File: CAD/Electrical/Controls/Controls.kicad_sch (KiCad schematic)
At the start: 31 parts, among them J1 Aileron Servo, J10 Battery and/or BMS, J11 Restart/Boot Button, J12 GPS, J13 Cadence Sensor, J14 Gyroscope, J15 LCD, J16 pitot tube assembly, J17 SD card selecting jumper, J18 SD card selecting jumper, J2 SD card, J3 External Connector, J4 Rudder Servo, J5 Elevator Servo, J6 BME280, J7 Pitch Control, J8 Roll Control, J9 SD card selecting jumper, U1 ESP32-C3-DevKitM-1, U2 Voltage regulator

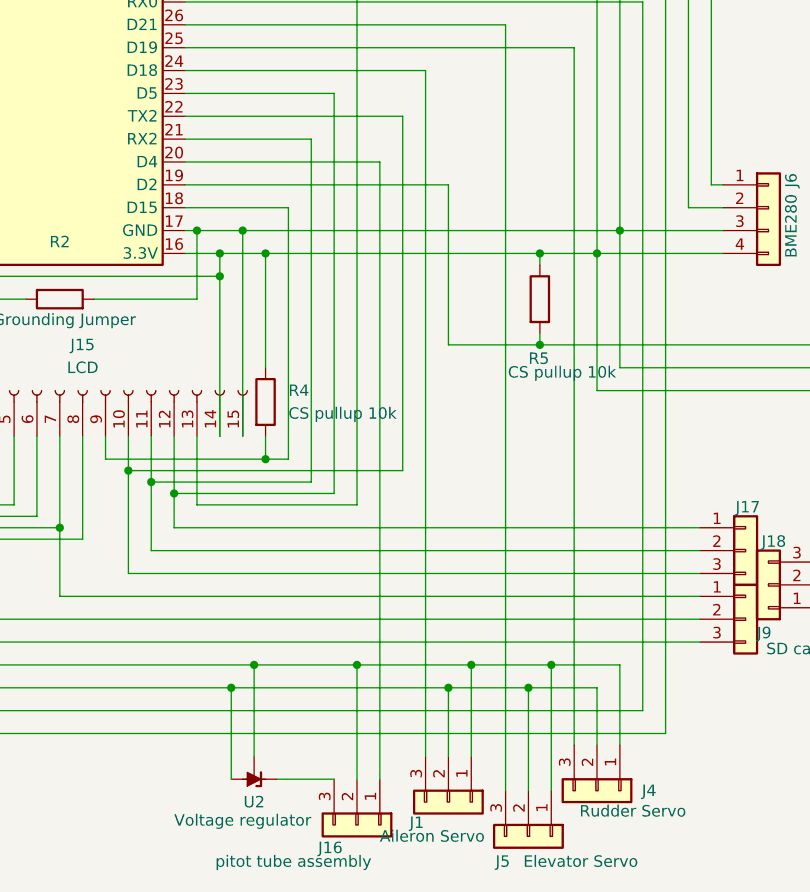
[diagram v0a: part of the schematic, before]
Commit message: Added more electrical components
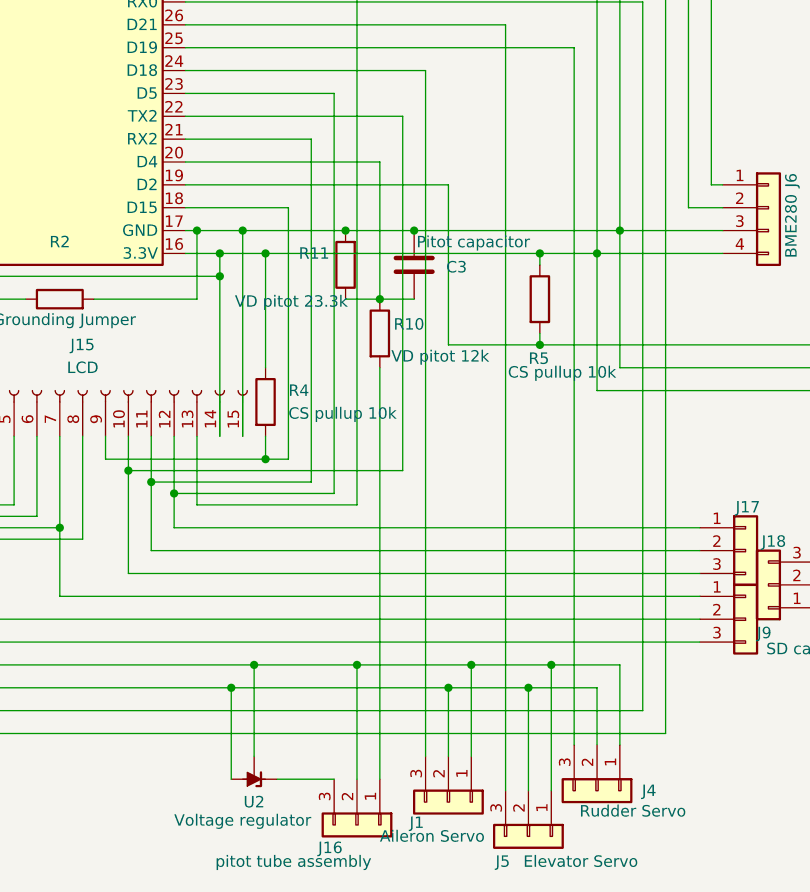
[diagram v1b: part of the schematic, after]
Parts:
- added C3: Pitot capacitor, Capacitor_SMD:C_0402_1005Metric_Pad0.74x0.62mm_HandSolder, symbol Device:C
- added R10: VD pitot 12k, OptoDevice:R_LDR_4.9x4.2mm_P2.54mm_Vertical, symbol Device:R
- added R11: VD pitot 23.3k, OptoDevice:R_LDR_4.9x4.2mm_P2.54mm_Vertical, symbol Device:R
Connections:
- net at J14.2 (Pin_2), J15.15 (Pin_15), J2.5 (Pin_5)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: now also C3.1, R11.2
- net at U1.20 (D4): now also C3.2, R10.1, R11.1; no longer J16.1 (Pin_1)
- new net: J16.1 (Pin_1), R10.2

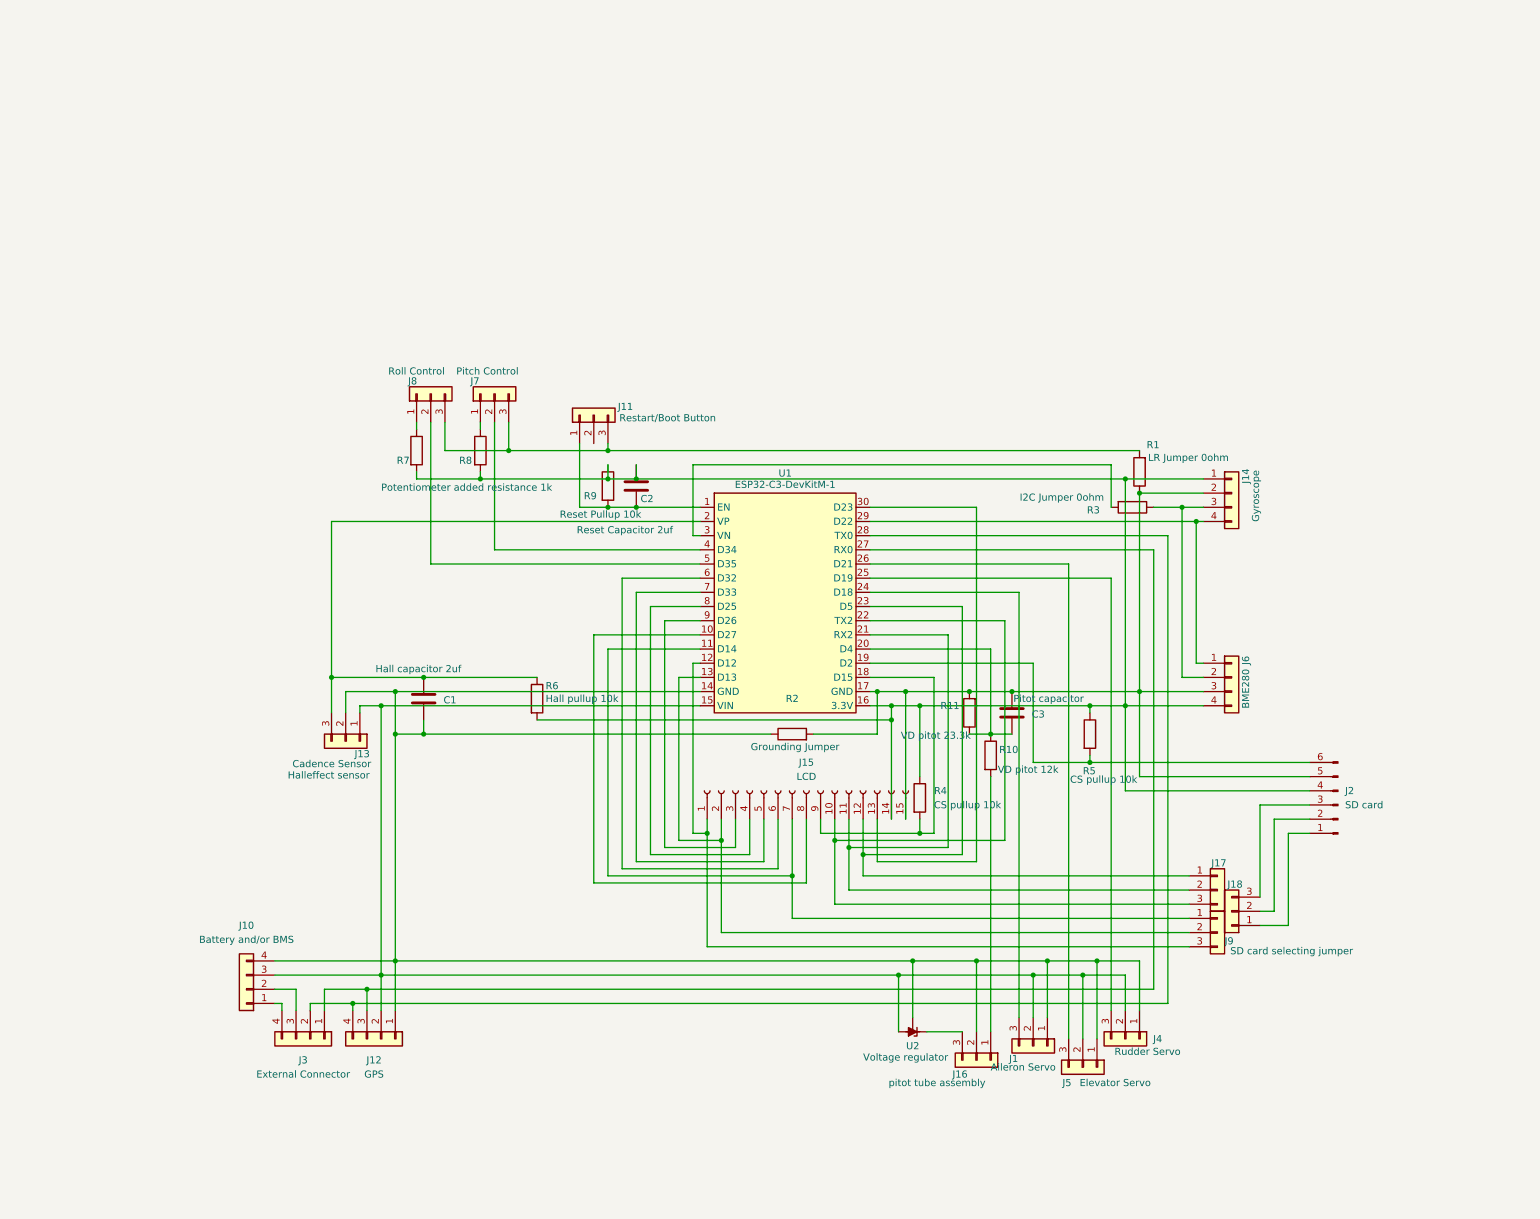
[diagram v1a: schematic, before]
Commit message: Mostly done schematic
the voltage regulators are done
need to rewire from dev board to esp32

then PCB drawing
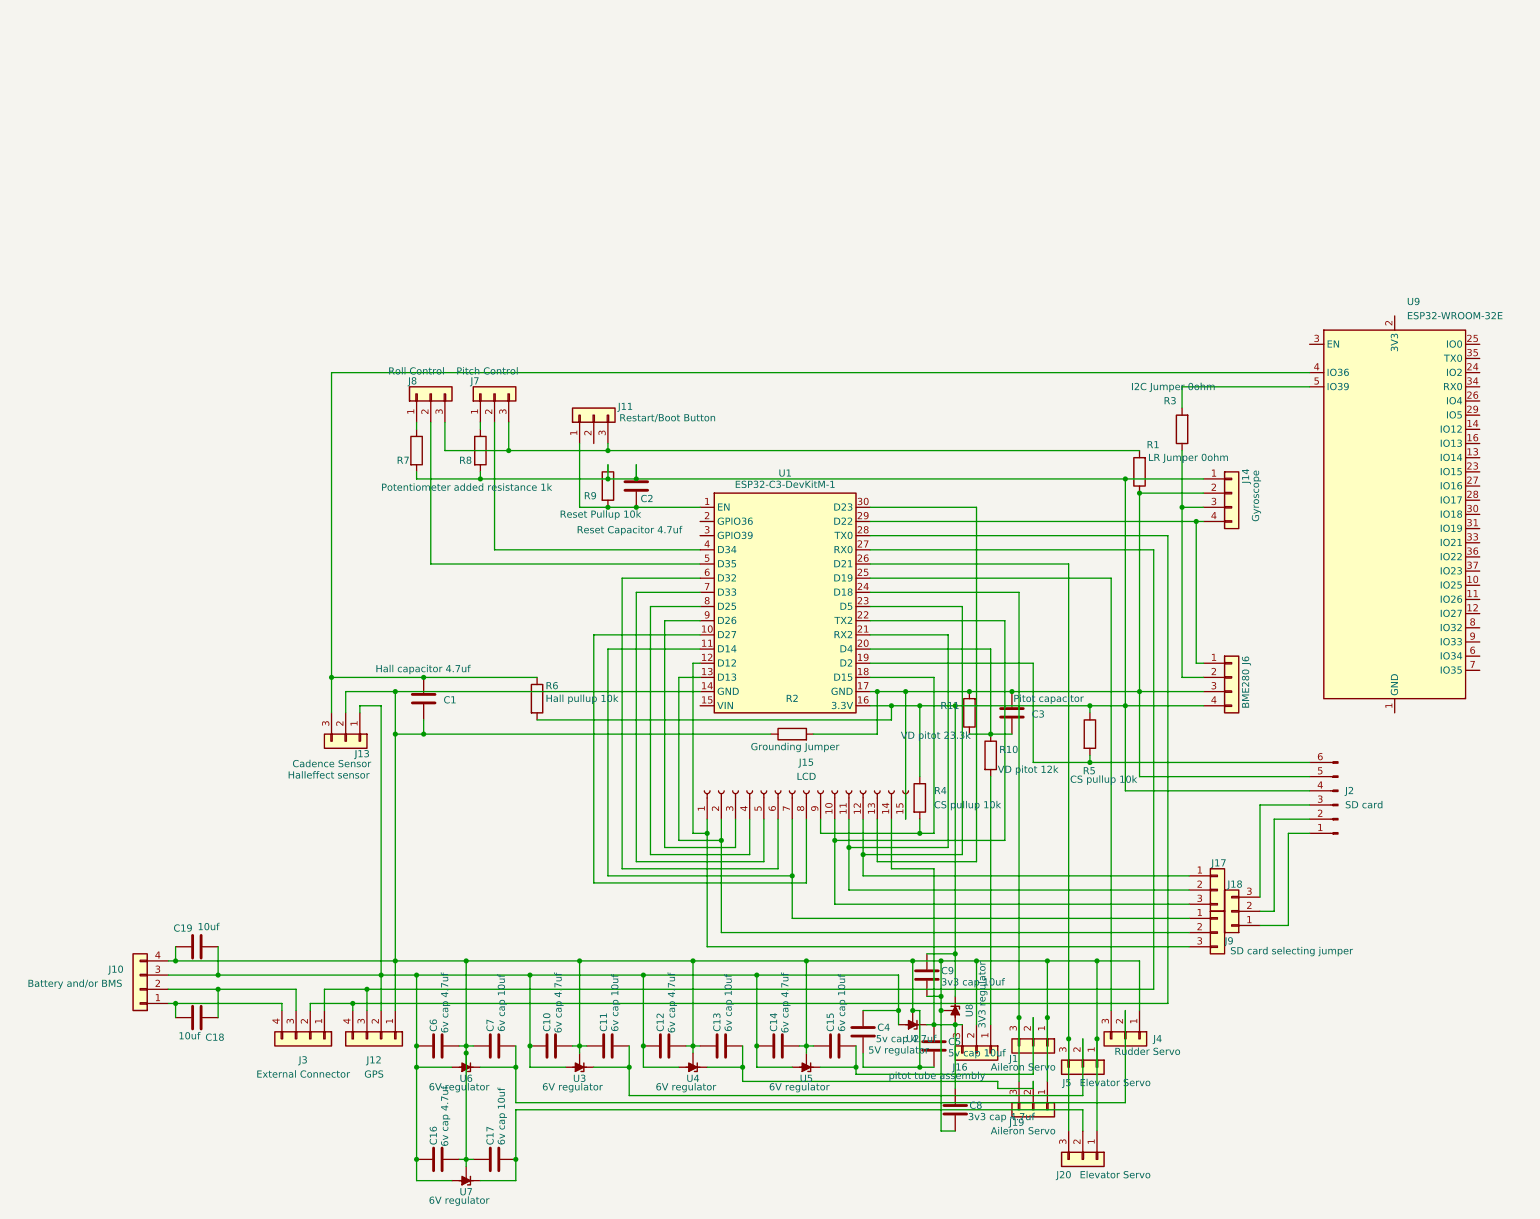
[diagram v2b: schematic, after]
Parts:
- added C10, C12, C14, C16, C6: 6v cap 4.7uf, Capacitor_SMD:C_0402_1005Metric_Pad0.74x0.62mm_HandSolder, symbol Device:C
- added C11, C13, C15, C17, C7: 6v cap 10uf, Capacitor_SMD:C_0402_1005Metric_Pad0.74x0.62mm_HandSolder, symbol Device:C
- added C18, C19: 10uf, Capacitor_SMD:C_0402_1005Metric_Pad0.74x0.62mm_HandSolder, symbol Device:C
- added C4: 5v cap 4.7uf, Capacitor_SMD:C_0402_1005Metric_Pad0.74x0.62mm_HandSolder, symbol Device:C
- added C5: 5v cap 10uf, Capacitor_SMD:C_0402_1005Metric_Pad0.74x0.62mm_HandSolder, symbol Device:C
- added C8: 3v3 cap 4.7uf, Capacitor_SMD:C_0402_1005Metric_Pad0.74x0.62mm_HandSolder, symbol Device:C
- added C9: 3v3 cap 10uf, Capacitor_SMD:C_0402_1005Metric_Pad0.74x0.62mm_HandSolder, symbol Device:C
- added J19: Aileron Servo, Connector_Molex:Molex_KK-254_AE-6410-03A_1x03_P2.54mm_Vertical, symbol Connector_Generic:Conn_01x03
- added J20: Elevator Servo, Connector_Molex:Molex_KK-254_AE-6410-03A_1x03_P2.54mm_Vertical, symbol Connector_Generic:Conn_01x03
- added U3, U4, U5, U6, U7: 6V regulator, Package_TO_SOT_SMD:TO-252-2, symbol Reference_Voltage:TL431KTP
- added U8: 3V3 regulator, Package_TO_SOT_SMD:TO-252-2, symbol Reference_Voltage:TL431KTP
- added U9: ESP32-WROOM-32E, RF_Module:ESP32-WROOM-32, symbol RF_Module:ESP32-WROOM-32E
- C1: value Hall capacitor 2uf -> Hall capacitor 4.7uf
- C2: value Reset Capacitor 2uf -> Reset Capacitor 4.7uf
- U2: value Voltage regulator -> 5V regulator
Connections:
- net at C1.2, J1.1 (Pin_1), J10.4 (Pin_4)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: now also C10.2, C11.1, C12.2, C13.1, C14.2, C15.1, C16.2, C17.1, C19.1, C4.2, C5.2, C6.2, C7.1, C8.2, C9.2, J19.1 (Pin_1), J20.1 (Pin_1), U3.1 (REF), U4.1 (REF), U5.1 (REF), U6.1 (REF), U7.1 (REF), U8.1 (REF)
- net at J10.3 (Pin_3), J12.2 (Pin_2), J13.1 (Pin_1)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: now also C10.1, C12.1, C14.1, C16.1, C19.2, C4.1, C6.1, U3.2 (A), U4.2 (A), U5.2 (A), U6.2 (A), U7.2 (A); no longer J1.2 (Pin_2), J4.2 (Pin_2), J5.2 (Pin_2), U1.15 (VIN)
- net at C2.1, J14.1 (Pin_1), J2.4 (Pin_4)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: now also C9.1, U8.3 (K); no longer J15.14 (Pin_14)
- net at C1.1, J13.3 (Pin_3), R6.1: now also U9.4 (IO36); no longer U1.2 (VP)
- net at R3.2: now also U9.5 (IO39); no longer U1.3 (VN)
- net at J5.3 (Pin_3), U1.26 (D21): now also J20.3 (Pin_3)
- net at J10.2 (Pin_2), J3.3 (Pin_3): now also C18.1
- net at J10.1 (Pin_1), J3.4 (Pin_4): now also C18.2
- net at J16.3 (Pin_3), U2.3 (K): now also J15.14 (Pin_14), C5.1, C8.1, U8.2 (A)
- net at J1.3 (Pin_3), U1.24 (D18): now also J19.3 (Pin_3)
- new net: C13.2, J19.2 (Pin_2), U4.3 (K)
- new net: C7.2, J4.2 (Pin_2), U6.3 (K)
- new net: C15.2, J1.2 (Pin_2), U5.3 (K)
- new net: C11.2, J5.2 (Pin_2), U3.3 (K)
- new net: C17.2, J20.2 (Pin_2), U7.3 (K)
- new net: U9.1 (GND), U9.15 (GND), U9.38 (GND), U9.39 (GND)
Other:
- moved on the sheet: J10, J16, R3, U2

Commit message: Schematic and almost BOM
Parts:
- removed C10, C12, C14, C16, C6: 6v cap 4.7uf, Capacitor_SMD:C_0402_1005Metric_Pad0.74x0.62mm_HandSolder, symbol Device:C
- removed C11, C13, C15, C17, C7: 6v cap 10uf, Capacitor_SMD:C_0402_1005Metric_Pad0.74x0.62mm_HandSolder, symbol Device:C
- removed J20: Elevator Servo, Connector_Molex:Molex_KK-254_AE-6410-03A_1x03_P2.54mm_Vertical, symbol Connector_Generic:Conn_01x03
- removed U3, U4, U5, U6, U7: 6V regulator, Package_TO_SOT_SMD:TO-252-2, symbol Reference_Voltage:TL431KTP
- added R12: 3.5k battery voltage divider, symbol Device:R
- added R13: 1k battery voltage divider, symbol Device:R
- added U3: 3-6V to 6V DC/DC converter, Converter_DCDC:Converter_DCDC_TRACO_TMU3-05xx_12xx_THT, symbol Converter_DCDC:TMU3-1212
- J1: value Aileron Servo -> Elevator Servo
- J19: value Aileron Servo -> Rudder Servo
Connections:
- net at C1.2, C9.2, J12.1 (Pin_1)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: now also C4.1, C5.1, C8.1, J1.3 (Pin_3), J19.3 (Pin_3), J4.3 (Pin_3), J5.3 (Pin_3), U3.3 (-Vout); no longer C19.1, C4.2, C5.2, C8.2, J1.1 (Pin_1), J10.4 (Pin_4), J19.1 (Pin_1), J4.1 (Pin_1), J5.1 (Pin_1)
- net at J19.2 (Pin_2): now also C4.2, J1.2 (Pin_2), J13.1 (Pin_1), J4.2 (Pin_2), J5.2 (Pin_2), U2.2 (A), U3.4 (+Vout)
- net at J15.14 (Pin_14), J16.3 (Pin_3), U2.3 (K)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: now also C5.2, C8.2, J12.2 (Pin_2); no longer C5.1, C8.1
- net at C1.1, J13.3 (Pin_3), R6.1: now also U1.2 (GPIO36); no longer U9.4 (IO36)
- net at R3.2: now also U1.26 (D21); no longer U9.5 (IO39)
- net at U1.25 (D19): now also J19.1 (Pin_1), J4.1 (Pin_1); no longer J4.3 (Pin_3)
- net at U1.3 (GPIO39): now also R12.1, R13.2
- new net: J1.1 (Pin_1), J5.1 (Pin_1), U1.24 (D18)
- new net: C19.1, J10.4 (Pin_4), R13.1, U3.2 (+Vin)
- new net: C19.2, J10.3 (Pin_3), R12.2, U3.1 (-Vin)
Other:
- moved on the sheet: C19, C4, C5, C8, C9, J5, R3, U2, U9

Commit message: schematics and weight update
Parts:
- removed J18, J9: SD card selecting jumper, symbol Connector_Generic:Conn_01x03
- added J20, J21: Elevron/Spoliron Servo, Connector_Molex:Molex_KK-254_AE-6410-03A_1x03_P2.54mm_Vertical, symbol Connector_Generic:Conn_01x03
- added J22: SD card selecting jumper, Connector_Hirose:Hirose_DF13-15P-1.25DSA_1x15_P1.25mm_Vertical, symbol Connector:Conn_01x15_Socket
- added Q1: 2N3904, Package_TO_SOT_THT:TO-92_Inline, symbol Transistor_BJT:2N3904
- added Q2: 2N3905, Package_TO_SOT_THT:TO-92_Inline, symbol Transistor_BJT:2N3905
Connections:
- net at C3.1, J14.2 (Pin_2), J2.5 (Pin_5)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: now also Q1.3 (C), Q2.3 (C); no longer J15.15 (Pin_15)
- net at C1.2, C4.1, C5.1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: now also C19.2, J10.3 (Pin_3), J15.15 (Pin_15), R12.2, U3.1 (-Vin), J20.3 (Pin_3), J21.3 (Pin_3), J22.15 (Pin_15)
- net at C5.2, C8.2, J12.2 (Pin_2)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: now also J22.14 (Pin_14)
- net at J15.1 (Pin_1), U1.12 (D12): now also J22.1 (Pin_1)
- net at J15.10 (Pin_10), U1.22 (TX2): now also J22.10 (Pin_10)
- net at J15.11 (Pin_11), U1.21 (RX2): now also J22.11 (Pin_11)
- net at J15.12 (Pin_12), U1.23 (D5): now also J22.12 (Pin_12)
- net at J15.13 (Pin_13), U1.30 (D23): now also J22.13 (Pin_13)
- net at J15.2 (Pin_2), U1.13 (D13): now also J22.2 (Pin_2)
- net at J15.3 (Pin_3), U1.9 (D26): now also J22.3 (Pin_3)
- net at J15.4 (Pin_4), U1.8 (D25): now also J22.4 (Pin_4)
- net at J15.5 (Pin_5), U1.7 (D33): now also J22.5 (Pin_5)
- net at J15.6 (Pin_6), U1.6 (D32): now also J22.6 (Pin_6)
- net at J15.7 (Pin_7), U1.11 (D14): now also J22.7 (Pin_7)
- net at J15.8 (Pin_8), U1.10 (D27): now also J22.8 (Pin_8)
- net at J15.9 (Pin_9), R4.2: now also J22.9 (Pin_9), Q1.1 (E); no longer U1.18 (D15)
- net at C4.2, J1.2 (Pin_2), J13.1 (Pin_1)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: now also J20.2 (Pin_2), J21.2 (Pin_2)
- net at J2.6 (Pin_6), R5.2: now also Q2.1 (E); no longer U1.19 (D2)
- new net: J20.1 (Pin_1), J21.1 (Pin_1), U1.19 (D2)
- new net: Q1.2 (B), Q2.2 (B), U1.18 (D15)
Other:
- moved on the sheet: C8, J1, J17, J19, J4, J5, U9
